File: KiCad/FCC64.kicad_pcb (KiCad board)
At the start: 2 copper layers, 58 x 84 mm, 50 parts, among them P1 JTAG, SW1 Reset, U1 27C256, U2 ATF1504AS, U3 W65C02S_TQFP, U4 ICS525-01, U5 27C256, U6 62256, U7 TPS3619-50, X1 12MHz, Y1 C64-Expansionport

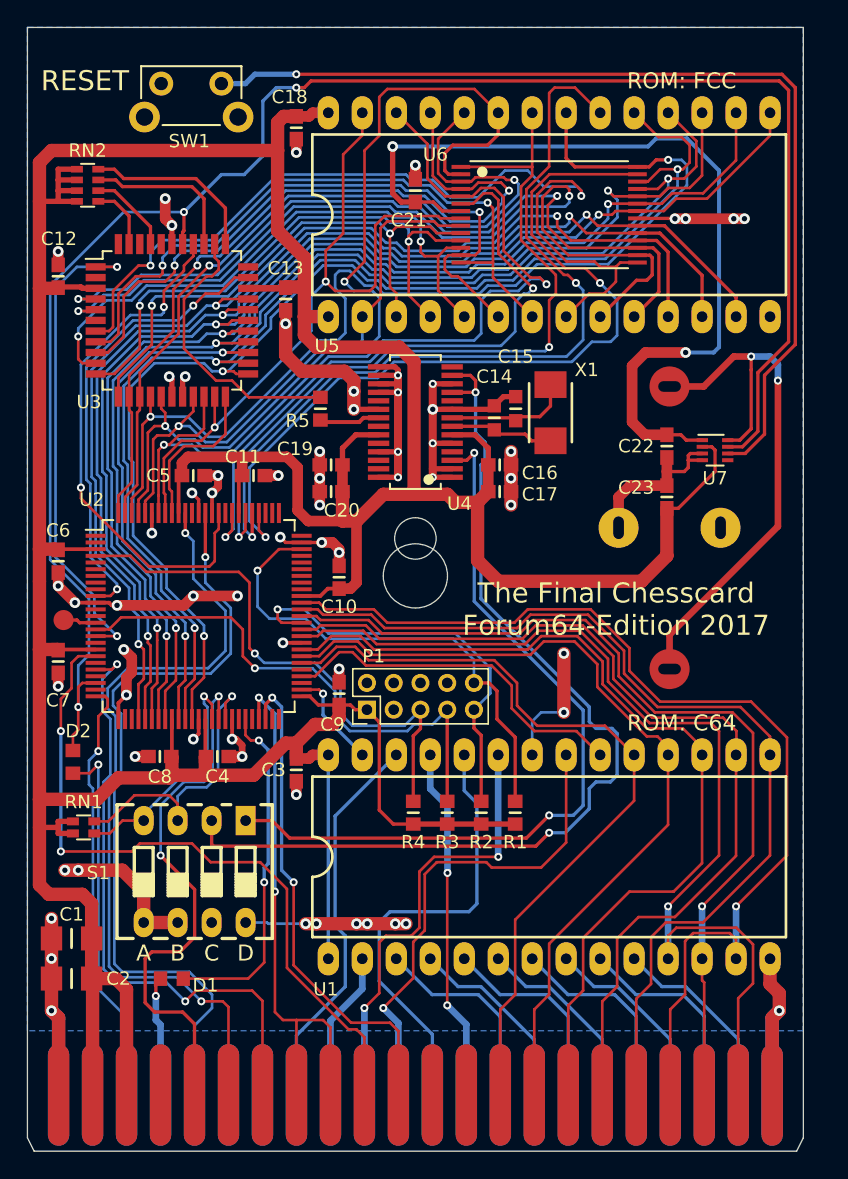
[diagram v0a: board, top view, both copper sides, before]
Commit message: Various issues solved:
* QFP44-Footprint for W65C02 corrected
* FCC-On/Off deleted
* new battery supervisor ic TPS6513-01
* Battery Holder corrected
* Signals D5 and D7 to CPLD swapped
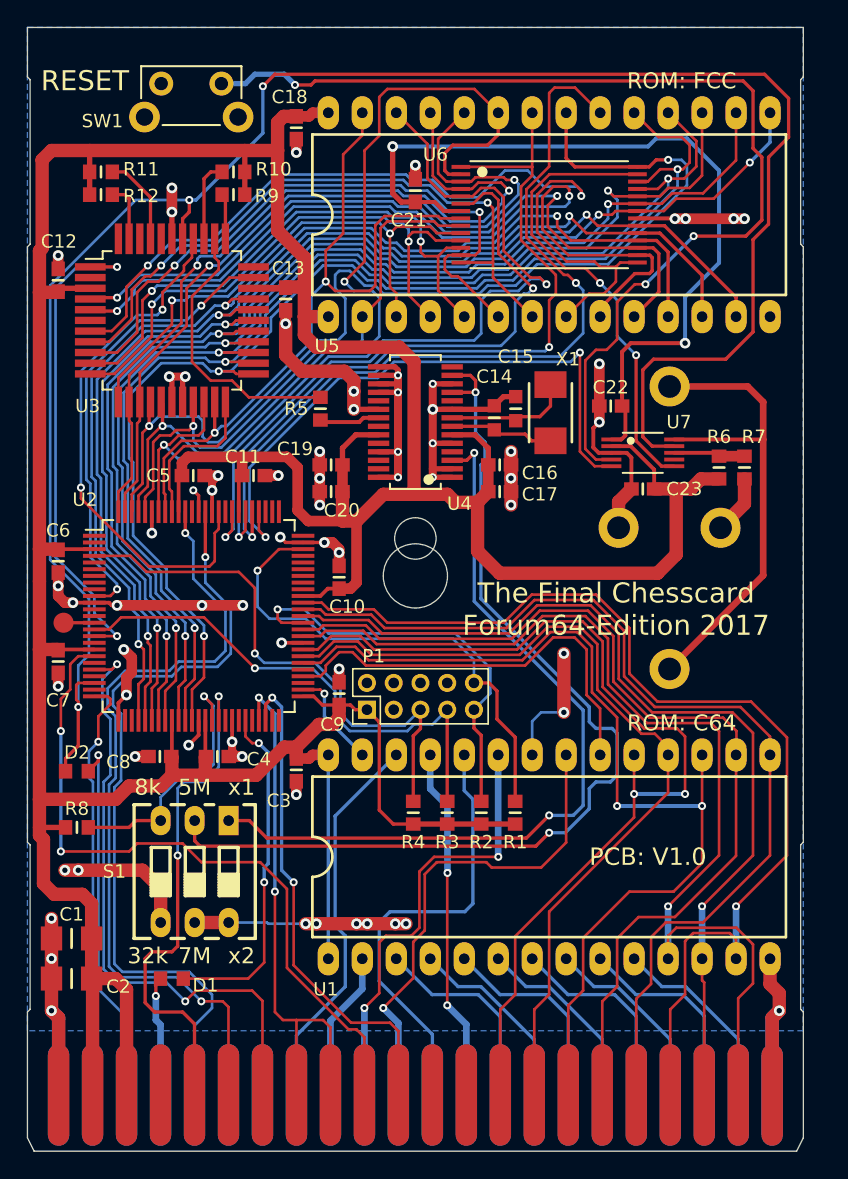
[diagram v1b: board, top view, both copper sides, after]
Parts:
- removed REF** (x2): X, TTB_MyLib:TTB_Hole3,2mm
- removed REF**: Measurement_Point_Round-SMD-Pad_Small, Measurement_Points:Measurement_Point_Round-SMD-Pad_Small
- removed RN1: 2k2, TTB_MyLib:TTB_RNet1206_2R
- removed RN2: 2k2, TTB_MyLib:TTB_RNet1206_4R
- added ?: Test, Measurement_Points:Measurement_Point_Round-SMD-Pad_Small, F.Cu at (113.7, 95.5)
- added R10: 2k2, TTB_MyLib:TTB_R0603, F.Cu at (126.4, 61.8)
- added R11: 2k2, TTB_MyLib:TTB_R0603, F.Cu at (116.5, 61.8)
- added R12: 2k2, TTB_MyLib:TTB_R0603, F.Cu at (116.5, 63.5)
- added R6: 3k4, TTB_MyLib:TTB_R0603, F.Cu at (162.7, 83.9)
- added R7: 1k15, TTB_MyLib:TTB_R0603, F.Cu at (164.6, 83.9)
- added R8: 2k2, TTB_MyLib:TTB_R0603, F.Cu at (114.7, 110.8)
- added R9: 2k2, TTB_MyLib:TTB_R0603, F.Cu at (126.4, 63.5)
- MH1: footprint TTB_MyLib:TTB_Hole3,2mm -> TTB_MyLib:TTB_Hole4,8mm
- MH2: footprint TTB_MyLib:TTB_Hole3,2mm -> TTB_MyLib:TTB_Hole3,1mm
- R1, R2, R3, R4: value dnp -> 100k
- S1: footprint TTB_MyLib:TTB_DIPSwitch4 -> TTB_MyLib:TTB_DIPSwitch3
- U2: footprint Housings_QFP:TQFP-100_14x14mm_Pitch0.5mm -> TTB_MyLib:TTB_TQFP100
- U3: footprint Housings_QFP:TQFP-44_10x10mm_Pitch0.8mm -> TTB_MyLib:TTB_W65C02
- U7: value TPS3619-50 -> TPS3613-01; footprint Housings_DFN_QFN:DFN-8_2x2mm_Pitch0.5mm -> TTB_MyLib:TTB_MSOP10
- moved U7 5.40 mm to (157.0, 82.8), turned to 270 degrees
- moved C22 5.16 mm to (154.6, 79.3), turned to 180 degrees
- moved C23 1.90 mm to (157.0, 85.5), turned to 180 degrees
- moved D2 0.76 mm to (114.7, 106.6), turned to 0 degrees
- moved C12 0.30 mm to (113.3, 69.9)
- turned MH1 to 0 degrees
- turned MH2 to 0 degrees
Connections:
- S1 pad 3: SW-FCC_ON -> SW-RAMSIZE
- S1 pad 4: SW-RAMSIZE -> GND
- U2 pad 42: SW-FCC_ON -> (no net)
- U2 pad 56: /C64/D7 -> /C64/D5
- U2 pad 58: /C64/D5 -> /C64/D7
- U2 pad 79: ~RAM_CE -> ~RAM_SEL
- U7 pad 4: GND -> Net-(SW1-Pad2)
- U7 pad 5: Net-(U7-Pad5) -> ~RAM_SEL
- U7 pad 6: Net-(SW1-Pad2) -> ~RAM_CE
- U7 pad 7: ~Reset -> Net-(U7-Pad7)
- U7 pad 8: Net-(BT1-Pad1) -> Net-(R6-Pad2)
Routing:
- net ~RAM_SEL: track 0.00 -> 46.3 mm, vias 0 -> 2
- net ~RAM_CE: track 62.0 -> 34.8 mm
- net SW-FCC_ON: track 22.3 -> 0.00 mm, vias 1 -> 0
- net /C64/D7: track 59.3 -> 73.5 mm, vias 0 -> 2
- net GND: track 206.0 -> 218.7 mm, vias 64 -> 66
- net Net-(R9-Pad1): track 13.4 -> 3.40 mm
- net ~Reset: track 135.2 -> 144.6 mm
- net /C64/D5: track 67.7 -> 74.4 mm, vias 0 -> 2
- net Net-(BT1-Pad1): track 42.9 -> 37.0 mm, vias 2 -> 0
- net Net-(R10-Pad1): track 11.9 -> 6.06 mm
- net Net-(R6-Pad2): track 0.00 -> 5.35 mm
- net Net-(SW1-Pad2): track 73.8 -> 78.8 mm, vias 1 -> 3
- net ~ROM1_CE: track 27.2 -> 32.1 mm
- net Net-(C21-Pad2): track 65.1 -> 61.3 mm
- net +5V: track 342.5 -> 339.4 mm
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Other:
- outline, holes or cut-outs redrawn
- rule pad_to_mask_clearance: 0 -> 0.02
- board text added: "32k"
- board text added: "5M"
- board text added: "7M"
- board text added: "8k"
- board text added: "CPU Speed RAM 8k/32k"
- board text added: "PCB: V1.0"
- board text added: "x1"
- board text added: "x2"
- board text removed: "A"
- board text removed: "B"
- board text removed: "C"
- board text removed: "D"
- board text removed: "RAM 8k/32k CPU Speed FCC On/Off"

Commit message: Tidying up for initial batch
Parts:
- C1, C2: value 4µ7 -> 10µ
- moved Y1 0.10 mm to (140.0, 130.7)
- turned S1 to 0 degrees
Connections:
- S1 pad 1: SW-CLKB -> GND
- S1 pad 2: SW-CLKA -> GND
- S1 pad 3: SW-RAMSIZE -> GND
- S1 pad 4: GND -> SW-CLKB
- S1 pad 5: GND -> SW-CLKA
- S1 pad 6: GND -> SW-RAMSIZE
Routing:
- net GND: track 218.7 -> 223.1 mm, vias 66 -> 68
- net /6502/intPHI2O: track 39.9 -> 37.9 mm
- net Net-(P1-Pad10): track 37.1 -> 36.3 mm
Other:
- board text added: "Designed 2017 by Freak"
- board text removed: "Design by Freak"
